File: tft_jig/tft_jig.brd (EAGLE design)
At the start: 47.5 x 61.5 mm, 23 parts, among them J1 SPI, J2 PJ-030DH-SMT-TR, U1 CD74HC238PWR, U2 74HC4051, U3 LM2576SX-5.0/NOPB

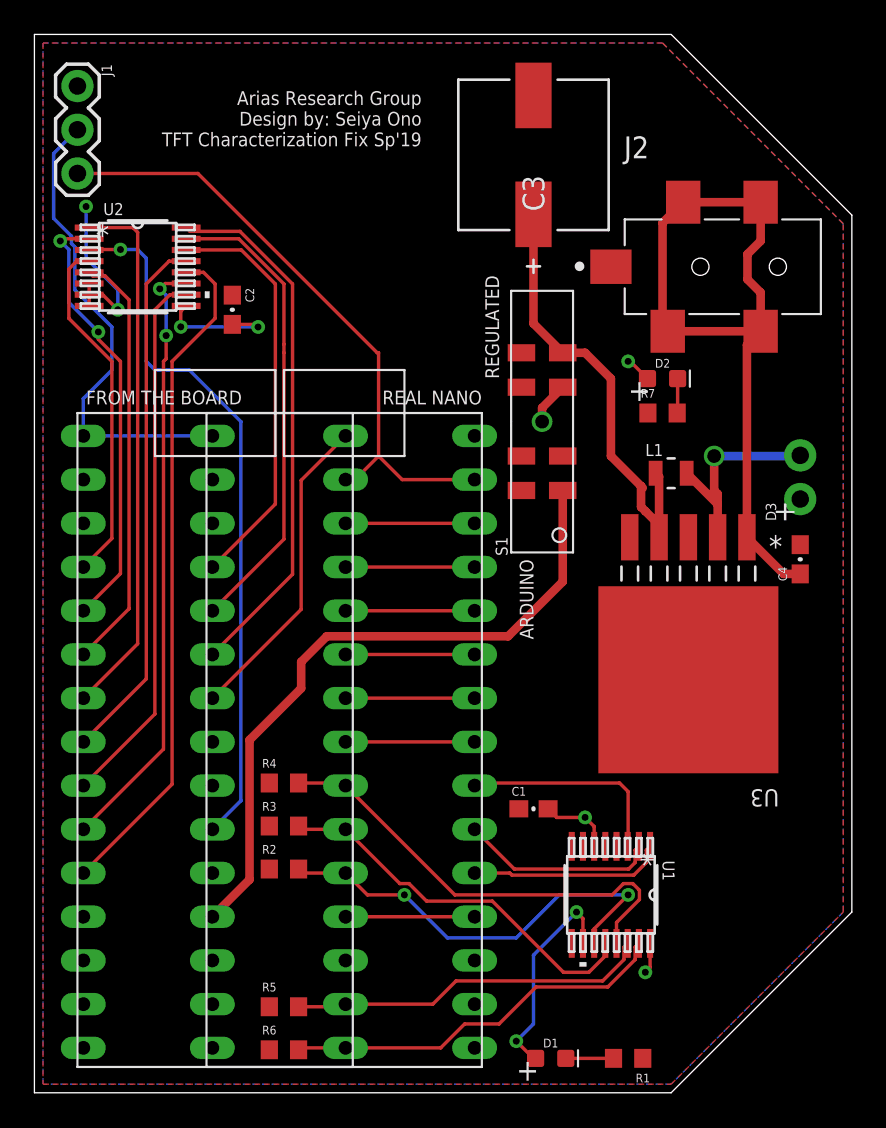
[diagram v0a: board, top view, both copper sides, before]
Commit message: fix vcc cap
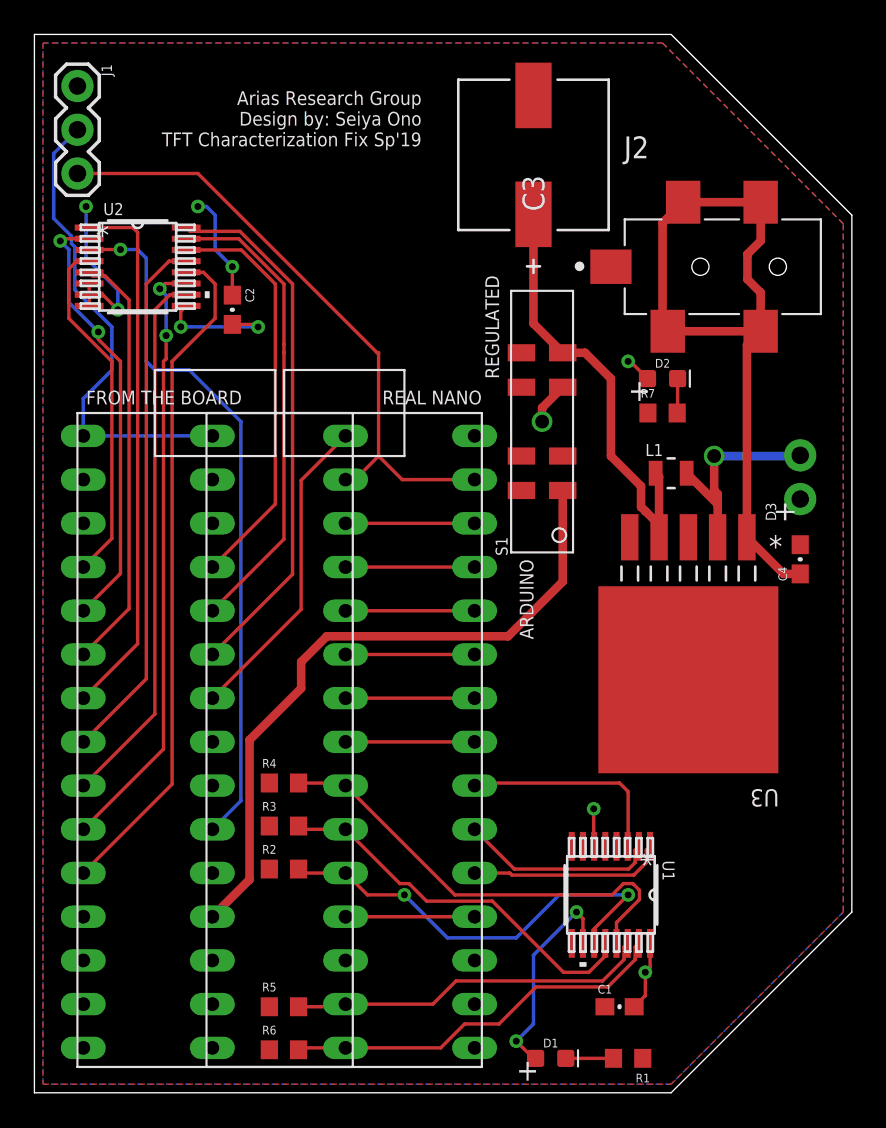
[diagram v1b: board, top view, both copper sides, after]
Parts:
- C4: value 1mF -> 0.1uF
- moved C1 12.5 mm to (34.0, 5.00)
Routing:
- net GND: track 10.1 -> 16.4 mm, vias 2 -> 4
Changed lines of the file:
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@@
 </autorouter>
 <elements>
-<element name="C1" library="scono" package="0603-CAP" value="0.1uF" x="29" y="16.5" smashed="yes">
-<attribute name="NAME" x="27.73" y="17.262" size="0.508" layer="25" font="vector" ratio="10"/>
-<attribute name="PIE-INT-REF-NUM" value="CAPACITOR-GENERIC" x="77.26" y="-43.19" size="1.778" layer="27" display="off"/>
-<attribute name="VALUE" x="27.73" y="15.103" size="0.508" layer="27" font="vector"/>
+<element name="C1" library="scono" package="0603-CAP" value="0.1uF" x="34" y="5" smashed="yes">
+<attribute name="NAME" x="32.73" y="5.762" size="0.508" layer="25" font="vector" ratio="10"/>
+<attribute name="PIE-INT-REF-NUM" value="CAPACITOR-GENERIC" x="82.26" y="-54.69" size="1.778" layer="27" display="off"/>
+<attribute name="VALUE" x="32.73" y="3.603" size="0.508" layer="27" font="vector"/>
 </element>
 <element name="C2" library="scono" package="0603-CAP" value="0.1uF" x="11.5" y="45.5" smashed="yes" rot="R270">
@@
 <attribute name="VENDOR" value="Nichicon" x="74.72" y="93.87" size="1.778" layer="27" rot="R90" display="off"/>
 </element>
-<element name="C4" library="scono" package="0603-CAP" value="1mF" x="44.5" y="31" smashed="yes" rot="R90">
+<element name="C4" library="scono" package="0603-CAP" value="0.1uF" x="44.5" y="31" smashed="yes" rot="R90">
 <attribute name="NAME" x="43.738" y="29.73" size="0.508" layer="25" font="vector" ratio="10" rot="R90"/>
 <attribute name="PIE-INT-REF-NUM" value="CAPACITOR-GENERIC" x="104.19" y="89.42" size="1.778" layer="27" rot="R90" display="off"/>
@@
 <vertex x="0.5" y="61"/>
 </polygon>
-<wire x1="11.5" y1="46.35" x2="4.8444" y2="46.6556" width="0" layer="19" extent="1-16"/>
+<wire x1="11.5" y1="46.35" x2="11.5" y2="48" width="0.2" layer="1"/>
+<via x="11.5" y="48" extent="1-16" drill="0.4"/>
+<wire x1="11.5" y1="48" x2="10.5" y2="49" width="0.2" layer="16"/>
+<wire x1="10.5" y1="49" x2="10.5" y2="51" width="0.2" layer="16"/>
+<wire x1="10.5" y1="51" x2="10" y2="51.5" width="0.2" layer="16"/>
+<wire x1="10" y1="51.5" x2="9.5" y2="51.5" width="0.2" layer="16"/>
+<via x="9.5" y="51.5" extent="1-16" drill="0.4"/>
 </signal>
 <signal name="S">
@@
 <vertex x="0.5" y="0.5"/>
 </polygon>
-<wire x1="32.525" y1="14.3194" x2="32.525" y2="15.475" width="0.2" layer="1"/>
-<wire x1="32.525" y1="15.475" x2="32" y2="16" width="0.2" layer="1"/>
-<via x="32" y="16" extent="1-16" drill="0.4"/>
 <wire x1="35.775" y1="8.6806" x2="35.775" y2="7.275" width="0.2" layer="1"/>
 <wire x1="35.775" y1="7.275" x2="35.5" y2="7" width="0.2" layer="1"/>
 <via x="35.5" y="7" extent="1-16" drill="0.4"/>
-<wire x1="29.85" y1="16.5" x2="30.35" y2="16" width="0.2" layer="1"/>
-<wire x1="30.35" y1="16" x2="32" y2="16" width="0.2" layer="1"/>
 <wire x1="30.7" y1="41" x2="29.5" y2="39.8" width="0.5" layer="1"/>
 <wire x1="29.5" y1="39.8" x2="29.5" y2="39" width="0.5" layer="1"/>
@@
 <wire x1="34.623" y1="42.5" x2="34.5" y2="42.5" width="0.2" layer="1"/>
 <via x="34.5" y="42.5" extent="1-16" drill="0.4"/>
+<wire x1="34.85" y1="5" x2="35.5" y2="5.65" width="0.2" layer="1"/>
+<wire x1="35.5" y1="5.65" x2="35.5" y2="7" width="0.2" layer="1"/>
+<wire x1="32.525" y1="14.3194" x2="32.5" y2="14.3444" width="0.2" layer="1"/>
+<wire x1="32.5" y1="14.3444" x2="32.5" y2="16.5" width="0.2" layer="1"/>
+<via x="32.5" y="16.5" extent="1-16" drill="0.4"/>
 </signal>
 <signal name="N$6">
@@
 <contactref element="D3" pad="2"/>
 <wire x1="39.7018" y1="34.7982" x2="39.7018" y2="34.1998" width="0.5" layer="1"/>
-<wire x1="39.7018" y1="33" x2="39.7018" y2="32.2804" width="0.5" layer="1"/>
 <wire x1="44.5" y1="37.04" x2="44.46" y2="37" width="0.5" layer="16"/>
 <wire x1="44.46" y1="37" x2="39.5" y2="37" width="0.5" layer="16"/>
@@
 <wire x1="39.5" y1="37" x2="39.5" y2="35" width="0.5" layer="1"/>
 <wire x1="39.5" y1="35" x2="39.7018" y2="34.7982" width="0.5" layer="1"/>
-<wire x1="39.35" y1="36.85" x2="39.5" y2="37" width="0.5" layer="1"/>
 <contactref element="L1" pad="2"/>
 <wire x1="37.9016" y1="36" x2="39.7018" y2="34.1998" width="0.5" layer="1"/>
-<wire x1="39.7018" y1="34.1998" x2="39.7018" y2="33" width="0.5" layer="1"/>
+<wire x1="39.7018" y1="34.1998" x2="39.7018" y2="32.2804" width="0.5" layer="1"/>
 </signal>
 <signal name="5V_REG">
@@
 <contactref element="U3" pad="4"/>
 <contactref element="S1" pad="4"/>
-<wire x1="36.5" y1="32.4822" x2="36.2982" y2="32.2804" width="0.5" layer="1"/>
 <wire x1="33.5" y1="37" x2="33.5" y2="41.5" width="0.5" layer="1"/>
 <wire x1="33.5" y1="41.5" x2="32" y2="43" width="0.5" layer="1"/>
 <wire x1="32" y1="43" x2="30.7" y2="43" width="0.5" layer="1"/>
-<wire x1="35.35" y1="35.15" x2="35.25" y2="35.25" width="0.5" layer="1"/>
 <wire x1="35.25" y1="35.25" x2="33.5" y2="37" width="0.5" layer="1"/>
 <wire x1="29" y1="51.0456" x2="29" y2="44.7" width="0.5" layer="1"/>
